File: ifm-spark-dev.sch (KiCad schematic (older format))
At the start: 5 parts

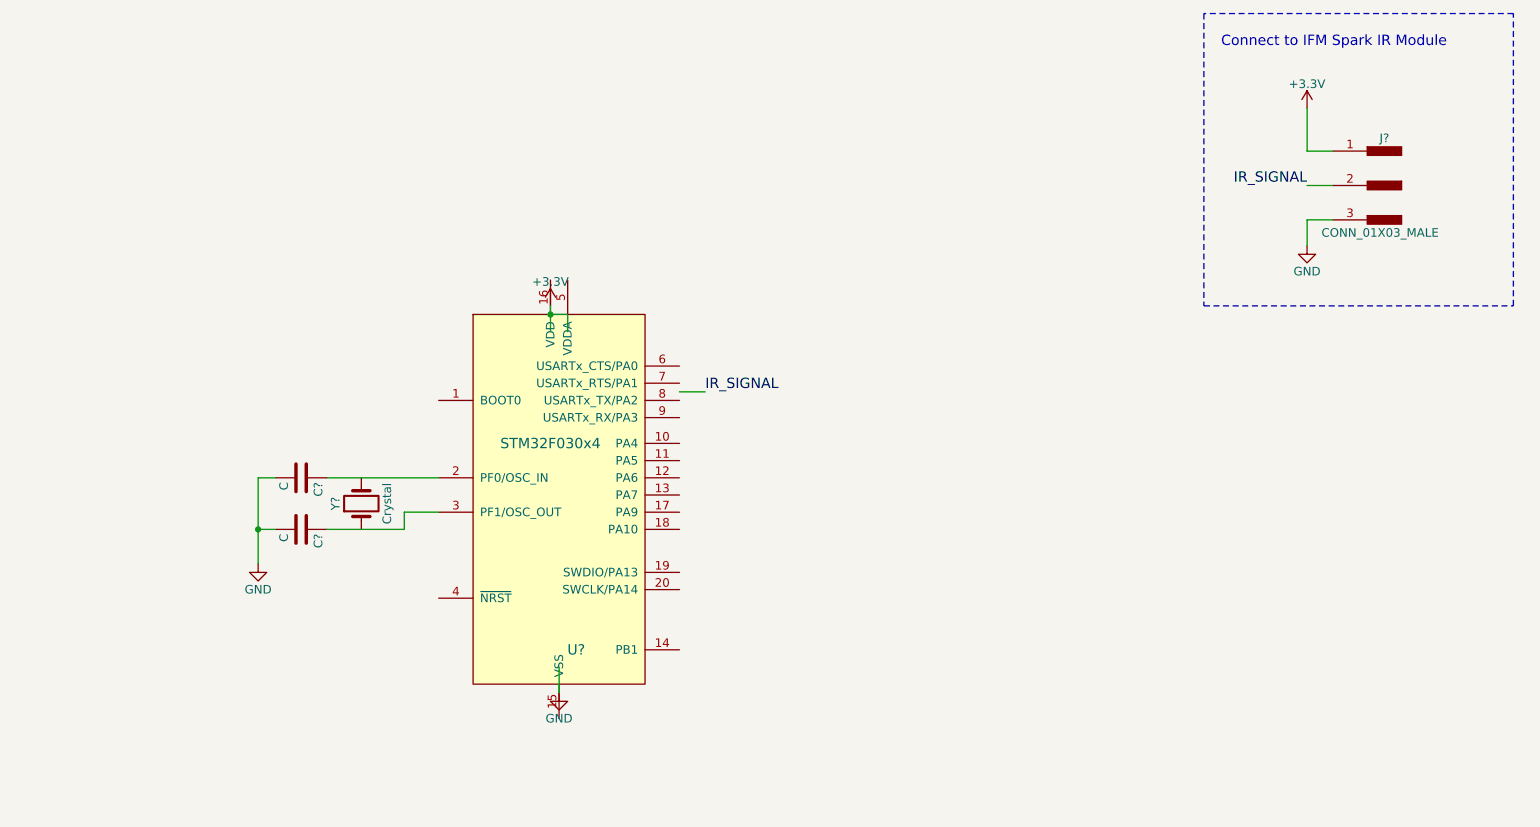
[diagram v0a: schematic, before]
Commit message: More connections, added a power LED indicator
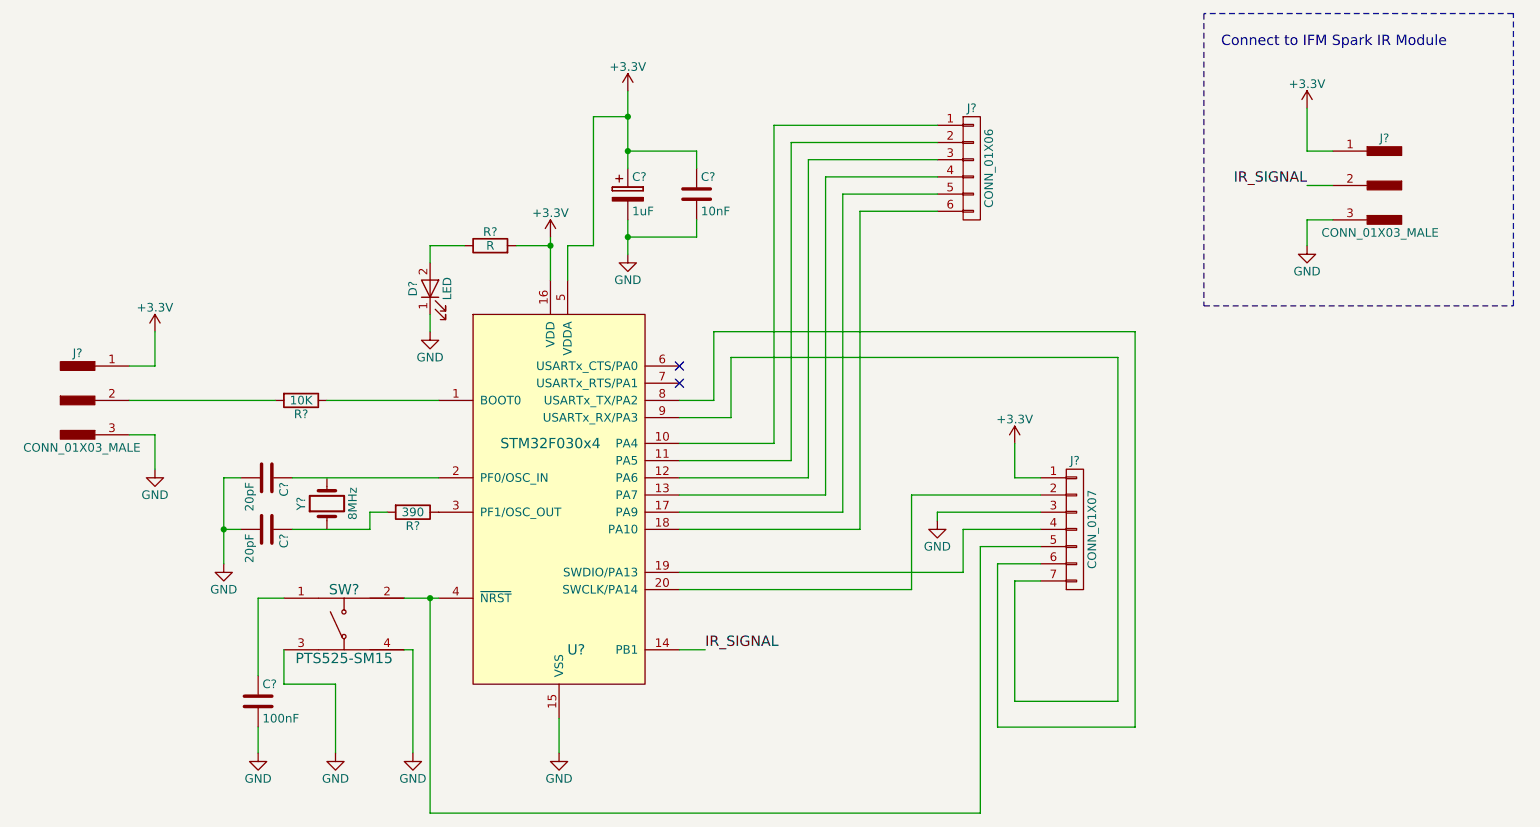
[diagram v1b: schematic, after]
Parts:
- added C?: 10nF, symbol C
- added C?: 1uF, symbol CP
- added C?: 100nF, symbol C
- added D?: LED, symbol LED
- added J?: CONN_01X03_MALE, symbol CONN_01X03_MALE
- added J?: CONN_01X07, symbol CONN_01X07
- added J?: CONN_01X06, symbol CONN_01X06
- added R?: 390, symbol R
- added R?: 10K, symbol R
- added R?: R, symbol R
- added SW?: PTS525-SM15, symbol PTS525-SM15
- C? (x2): value C -> 20pF
- U?: DKPN (none) -> 497-14044-5-ND; MPN (none) -> STM32F030F4P6
- Y?: value Crystal -> 8MHz
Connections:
- wire segments 19 -> 96
- no-connect marks 0 -> 2
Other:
- moved on the sheet: C?, Y?

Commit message: Untangle some wires
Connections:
- net BOOT0: now reaches R?.1, U?.1 (BOOT0)
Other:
- moved on the sheet: J?
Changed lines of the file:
@@
 L CONN_01X07 J?
 U 1 1 592A6D68
-P 8550 3650
-F 0 "J?" H 8550 4050 50  0000 C CNN
-F 1 "CONN_01X07" V 8650 3650 50  0000 C CNN
-F 2 "" H 8550 3650 50  0001 C CNN
-F 3 "" H 8550 3650 50  0001 C CNN
-	1    8550 3650
+P 8900 3650
+F 0 "J?" H 8900 4050 50  0000 C CNN
+F 1 "CONN_01X07" V 9000 3650 50  0000 C CNN
+F 2 "" H 8900 3650 50  0001 C CNN
+F 3 "" H 8900 3650 50  0001 C CNN
+	1    8900 3650
 	1    0    0    -1
 $EndComp
@@
 L +3.3V #PWR?
 U 1 1 592A6DD6
-P 8200 3150
-F 0 "#PWR?" H 8200 3000 50  0001 C CNN
-F 1 "+3.3V" H 8200 3290 50  0000 C CNN
-F 2 "" H 8200 3150 50  0001 C CNN
-F 3 "" H 8200 3150 50  0001 C CNN
-	1    8200 3150
+P 8500 3150
+F 0 "#PWR?" H 8500 3000 50  0001 C CNN
+F 1 "+3.3V" H 8500 3290 50  0000 C CNN
+F 2 "" H 8500 3150 50  0001 C CNN
+F 3 "" H 8500 3150 50  0001 C CNN
+	1    8500 3150
 	1    0    0    -1
 $EndComp
 Wire Wire Line
-	8350 3350 8200 3350
+	8700 3350 8500 3350
 Wire Wire Line
-	8200 3350 8200 3150
+	8500 3350 8500 3150
 Wire Wire Line
-	8350 3450 7600 3450
+	8700 3450 7600 3450
 Wire Wire Line
 	7600 3450 7600 4000
@@
 	7600 4000 6250 4000
 Wire Wire Line
-	7750 3550 8350 3550
+	7750 3550 8700 3550
 Wire Wire Line
-	8350 3650 7900 3650
+	8700 3650 7900 3650
 Wire Wire Line
 	7900 3650 7900 3900
@@
 	7750 3550 7750 3600
 Wire Wire Line
-	8350 3750 8000 3750
+	8700 3750 8000 3750
 Wire Wire Line
 	8000 3750 8000 5300
@@
 Connection ~ 4800 4050
 Wire Wire Line
-	8350 3850 8100 3850
+	8700 3850 8100 3850
 Wire Wire Line
 	8100 3850 8100 4800
 Wire Wire Line
-	8100 4800 8900 4800
+	8100 4800 9200 4800
 Wire Wire Line
-	8900 4800 8900 2500
+	9200 4800 9200 2400
 Wire Wire Line
-	8900 2500 6450 2500
+	9200 2400 6500 2400
 Wire Wire Line
-	6450 2500 6450 2900
+	6500 2400 6500 2900
 Wire Wire Line
-	6450 2900 6250 2900
+	6500 2900 6250 2900
 Wire Wire Line
-	8350 3950 8200 3950
+	8700 3950 8200 3950
 Wire Wire Line
 	8200 3950 8200 4650
 Wire Wire Line
-	8200 4650 8800 4650
+	8200 4650 9100 4650
 Wire Wire Line
-	8800 4650 8800 2650
+	9100 4650 9100 2500
 Wire Wire Line
-	8800 2650 6550 2650
+	9100 2500 6600 2500
 Wire Wire Line
-	6550 2650 6550 3000
+	6600 2500 6600 3000
 Wire Wire Line
-	6550 3000 6250 3000
+	6600 3000 6250 3000
 NoConn ~ 6250 2700
 NoConn ~ 6250 2800
@@
 L CONN_01X06 J?
 U 1 1 592BABFC
-P 7950 1550
-F 0 "J?" H 7950 1900 50  0000 C CNN
-F 1 "CONN_01X06" V 8050 1550 50  0000 C CNN
-F 2 "" H 7950 1550 50  0001 C CNN
-F 3 "" H 7950 1550 50  0001 C CNN
-	1    7950 1550
+P 7950 2950
+F 0 "J?" H 7950 3300 50  0000 C CNN
+F 1 "CONN_01X06" V 8050 2950 50  0000 C CNN
+F 2 "" H 7950 2950 50  0001 C CNN
+F 3 "" H 7950 2950 50  0001 C CNN
+	1    7950 2950
 	1    0    0    -1
 $EndComp
@@
 	6250 3150 6800 3150
 Wire Wire Line
-	6800 3150 6800 1300
+	6800 3150 6800 2700
 Wire Wire Line
-	6800 1300 7750 1300
+	6800 2700 7750 2700
 Wire Wire Line
 	6250 3250 6900 3250
 Wire Wire Line
-	6900 3250 6900 1400
+	6900 3250 6900 2800
 Wire Wire Line
-	6900 1400 7750 1400
+	6900 2800 7750 2800
 Wire Wire Line
 	6250 3350 7000 3350
 Wire Wire Line
-	7000 3350 7000 1500
+	7000 3350 7000 2900
 Wire Wire Line
-	7000 1500 7750 1500
+	7000 2900 7750 2900
 Wire Wire Line
 	6250 3450 7100 3450
 Wire Wire Line
-	7100 3450 7100 1600
+	7100 3450 7100 3000
 Wire Wire Line
-	7100 1600 7750 1600
+	7100 3000 7750 3000
 Wire Wire Line
 	6250 3550 7200 3550
 Wire Wire Line
-	7200 3550 7200 1700
+	7200 3550 7200 3100
 Wire Wire Line
-	7200 1700 7750 1700
+	7200 3100 7750 3100
 Wire Wire Line
 	6250 3650 7300 3650
 Wire Wire Line
-	7300 3650 7300 1800
+	7300 3650 7300 3200
 Wire Wire Line
-	7300 1800 7750 1800
+	7300 3200 7750 3200
 $Comp
 L R R?
@@
 Wire Wire Line
 	4800 2400 4800 2500
+Text Label 4850 2900 2    60   ~ 0
+BOOT0
 $EndSCHEMATC
